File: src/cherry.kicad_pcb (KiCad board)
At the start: 2 copper layers, 51 x 21 mm, 4 parts

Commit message: wip: current layout state
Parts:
- removed H1, H2, H3, H4: MountingHole, Cherry:MountingHole_2.1mm_M2
- added C1: 10uF, Cherry:C_0805_2012Metric, F.Cu at (110.1, 83.0)
- added C10: 100nF, Cherry:C_0402_1005Metric, F.Cu at (120.2, 81.3)
- added C11: 100nF, Cherry:C_0402_1005Metric, F.Cu at (122.4, 81.3)
- added C12: 100nF, Cherry:C_0402_1005Metric, F.Cu at (118.0, 81.3)
- added C13: 100nF, Cherry:C_0402_1005Metric, F.Cu at (128.5, 83.4)
- added C14: 100nF, Cherry:C_0402_1005Metric, F.Cu at (130.7, 83.4)
- added C15: 10uF, Cherry:C_0805_2012Metric, F.Cu at (118.6, 83.4)
- added C16: 100nF, Cherry:C_0402_1005Metric, F.Cu at (124.6, 97.5)
- added C17: 100nF, Cherry:C_0402_1005Metric, F.Cu at (135.3, 95.9)
- added C18: 100nF, Cherry:C_0402_1005Metric, F.Cu at (137.5, 95.9)
- added C19: 10uF, Cherry:C_0805_2012Metric, F.Cu at (137.1, 98.2)
- added C2: 10uF, Cherry:C_0805_2012Metric, F.Cu at (110.1, 98.0)
- added C20: 100nF, Cherry:C_0402_1005Metric, F.Cu at (135.3, 85.1)
- added C21: 100nF, Cherry:C_0402_1005Metric, F.Cu at (137.5, 85.1)
- added C22: 100nF, Cherry:C_0402_1005Metric, F.Cu at (139.7, 85.1)
- added C23: 100nF, Cherry:C_0402_1005Metric, F.Cu at (141.9, 85.1)
- added C24: 100nF, Cherry:C_0402_1005Metric, F.Cu at (143.3, 82.5)
- added C25: 10uF, Cherry:C_0805_2012Metric, F.Cu at (135.9, 82.5)
- added C26: 100nF, Cherry:C_0402_1005Metric, F.Cu at (140.0, 98.2)
- added C27: 10uF, Cherry:C_0603_1608Metric, F.Cu at (142.8, 98.2)
- added C28: 100nF, Cherry:C_0402_1005Metric, F.Cu at (131.4, 95.2)
- added C3: 22uF, Cherry:C_0805_2012Metric, F.Cu at (110.1, 86.6)
- added C4: 22uF, Cherry:C_0805_2012Metric, F.Cu at (110.1, 94.4)
- added C5: 4.7uF, Cherry:C_0603_1608Metric, F.Cu at (125.7, 83.4)
- added C6: 100nF, Cherry:C_0402_1005Metric, F.Cu at (126.8, 97.5)
- added C7: 100nF, Cherry:C_0402_1005Metric, F.Cu at (129.0, 97.5)
- added C8: 100nF, Cherry:C_0402_1005Metric, F.Cu at (131.2, 97.5)
- added C9: 100nF, Cherry:C_0402_1005Metric, F.Cu at (133.4, 97.5)
- added D1: PWR, Cherry:LED_0603_1608Metric, F.Cu at (103.5, 83.8)
- added D2: CFG, Cherry:LED_0603_1608Metric, F.Cu at (103.5, 97.2)
- added D3: USER0, Cherry:LED_0603_1608Metric, F.Cu at (158.7, 89.5)
- added D4: USER1, Cherry:LED_0603_1608Metric, F.Cu at (158.7, 91.5)
- added FB1: BLM21AG601SH1D, Cherry:L_0805_2012Metric, F.Cu at (108.4, 90.5)
- added FB2: BLM21AG601SH1D, Cherry:L_0805_2012Metric, F.Cu at (122.2, 83.4)
- added J1: USB4085-GF-A, Cherry:USB_C_Receptacle_GCT_USB4085, F.Cu at (106.1, 87.5)
- added J2: PinHeader_2x24, Cherry:PinHeader_2x24_P2.54mm_Rows22.86mm, F.Cu at (130.6, 90.5)
- added J3: PinHeader_2x06, Cherry:PinHeader_2x06_P2.54mm_Vertical, F.Cu at (148.4, 90.5)
- added J4: PinHeader_1x06, Cherry:PinHeader_1x06_P2.54mm, F.Cu at (153.4, 81.6)
- added J5: PinHeader_1x06, Cherry:PinHeader_1x06_P2.54mm, F.Cu at (153.4, 99.4)
- added L1: 1uH, Cherry:L_0805_2012Metric, F.Cu at (113.4, 86.6)
- added L2: 1uH, Cherry:L_0805_2012Metric, F.Cu at (113.4, 94.4)
- added R1: 180k, Cherry:R_0402_1005Metric, F.Cu at (112.3, 88.9)
- added R10: 10k, Cherry:R_0402_1005Metric, F.Cu at (138.9, 82.5)
- added R11: 10k, Cherry:R_0402_1005Metric, F.Cu at (131.4, 85.9)
- added R12: 10k, Cherry:R_0402_1005Metric, F.Cu at (155.4, 92.9)
- added R13: 100, Cherry:R_0402_1005Metric, F.Cu at (139.7, 95.9)
- added R14: 1k, Cherry:R_0402_1005Metric, F.Cu at (106.0, 83.8)
- added R15: 1k, Cherry:R_0402_1005Metric, F.Cu at (106.0, 97.2)
- added R16: 1k, Cherry:R_0402_1005Metric, F.Cu at (155.9, 89.5)
- added R17: 1k, Cherry:R_0402_1005Metric, F.Cu at (155.9, 91.5)
- added R2: 39.2k, Cherry:R_0402_1005Metric, F.Cu at (114.4, 88.9)
- added R3: 100k, Cherry:R_0402_1005Metric, F.Cu at (112.3, 92.1)
- added R4: 100k, Cherry:R_0402_1005Metric, F.Cu at (114.4, 92.1)
- added R5: 5.1k, Cherry:R_0402_1005Metric, F.Cu at (108.4, 87.6)
- added R6: 5.1k, Cherry:R_0402_1005Metric, F.Cu at (108.4, 93.4)
- added R7: 12k, Cherry:R_0402_1005Metric, F.Cu at (117.8, 97.5)
- added R8: 10k, Cherry:R_0402_1005Metric, F.Cu at (124.6, 81.3)
- added R9: 10k, Cherry:R_0402_1005Metric, F.Cu at (141.1, 82.5)
- added SW1: RESET, Cherry:SW_Push_1P1T_NO_CK_KMR2, F.Cu at (157.6, 85.6)
- added SW2: USER, Cherry:SW_Push_1P1T_NO_CK_KMR2, F.Cu at (157.6, 95.4)
- added U1: FT2232HQ, Cherry:QFN-64-1EP_9x9mm_P0.5mm_EP4.35x4.35mm, F.Cu at (121.7, 90.5)
- added U2: ICE40LP8K-CM81, Cherry:BGA-81_9x9_8.0x8.0mm_P0.8mm, F.Cu at (139.0, 90.5)
- added U3: W25Q32JVSSIQ, Cherry:SOIC-8_3.9x4.9mm_P1.27mm, F.Cu at (131.4, 90.5)
- added U4: TPS62A02, Cherry:SOT-23-6, F.Cu at (113.4, 83.0)
- added U5: TPS62A02, Cherry:SOT-23-6, F.Cu at (113.4, 98.0)
- added X1: ASE-12.000MHZ-LC-T, Cherry:Oscillator_SMD_Abracon_ASE-4Pin_3.2x2.5mm, F.Cu at (121.2, 97.5)
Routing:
- removed copper zone on B.Cu, net GND
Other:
- board size 51 x 21 mm -> 61.2 x 26.1 mm

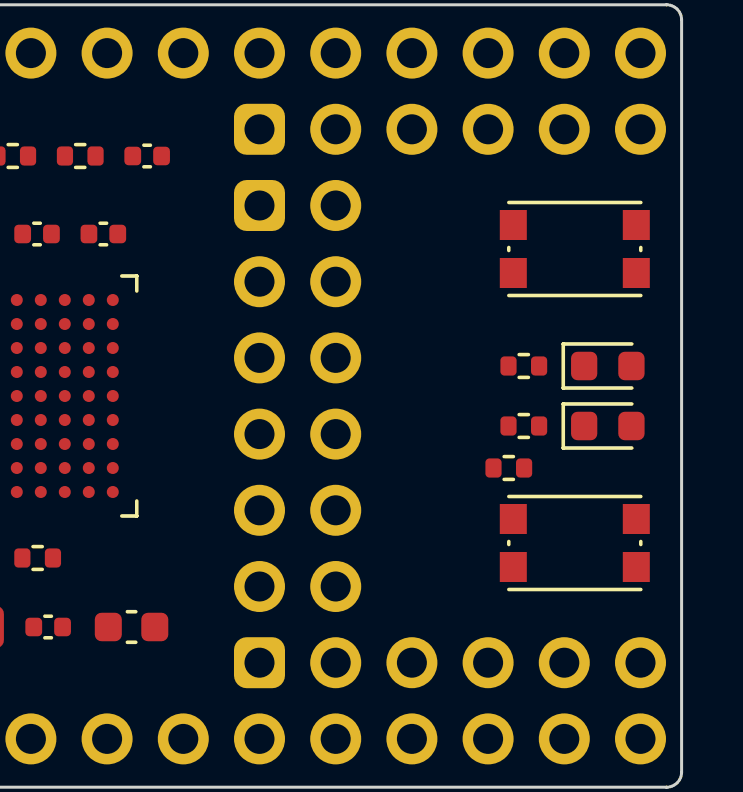
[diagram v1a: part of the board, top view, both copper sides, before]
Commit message: layout: J3を基板右端へ移動、SW/LEDを内側に再配置
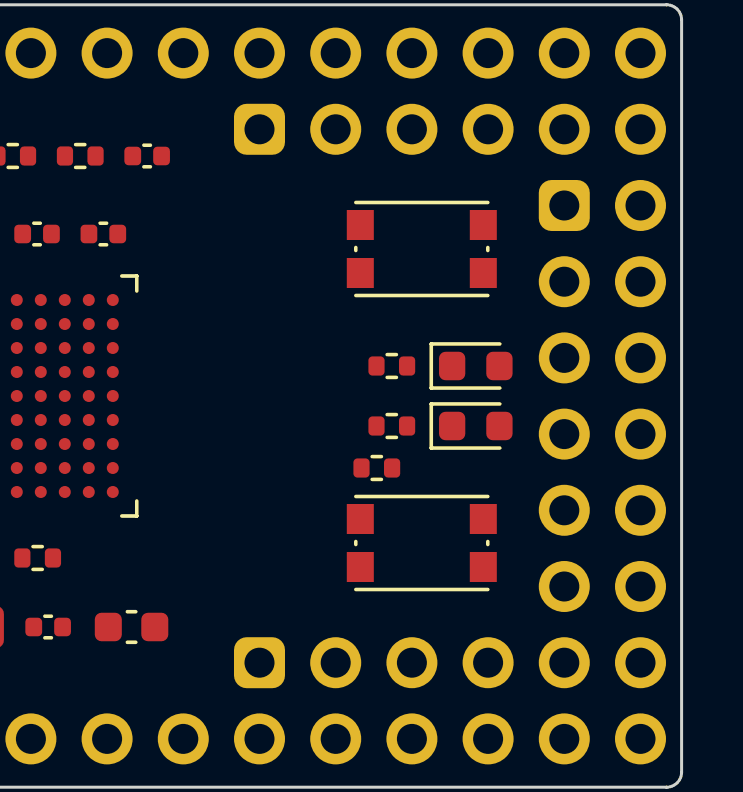
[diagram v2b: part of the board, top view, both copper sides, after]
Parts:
- moved J3 10.2 mm to (158.5, 90.5)
- moved SW1 5.10 mm to (152.5, 85.6)
- moved SW2 5.10 mm to (152.5, 95.4)
- moved R12 4.40 mm to (151.0, 92.9)
- moved R16 4.40 mm to (151.5, 89.5)
- moved R17 4.40 mm to (151.5, 91.5)
- moved D3 4.40 mm to (154.3, 89.5)
- moved D4 4.40 mm to (154.3, 91.5)
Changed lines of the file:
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@@
 	(footprint "Cherry:R_0402_1005Metric"
 		(layer "F.Cu")
-		(at 155.9 91.5)
+		(at 151.5 91.5)
 		(descr "Resistor SMD 0402 (1005 Metric), square (rectangular) end terminal, IPC-7351 nominal, (Body size source: IPC-SM-782 page 72, https://www.pcb-3d.com/wordpress/wp-content/uploads/ipc-sm-782a_amendment_1_and_2.pdf)")
 		(tags "resistor")
@@
 	(footprint "Cherry:LED_0603_1608Metric"
 		(layer "F.Cu")
-		(at 158.7 89.5)
+		(at 154.3 89.5)
 		(descr "LED SMD 0603 (1608 Metric), square (rectangular) end terminal, IPC-7351 nominal, (Body size source: http://www.tortai-tech.com/upload/download/2011102023233369053.pdf)")
 		(tags "LED")
@@
 	(footprint "Cherry:PinHeader_2x06_P2.54mm_Vertical"
 		(layer "F.Cu")
-		(at 148.36 90.5)
+		(at 158.52 90.5)
 		(descr "Pin header 2x06, 2.54mm pitch, vertical, odd-even numbering, origin at center")
 		(tags "pin header 2x06")
@@
 	(footprint "Cherry:SW_Push_1P1T_NO_CK_KMR2"
 		(layer "F.Cu")
-		(at 157.6 85.6)
+		(at 152.5 85.6)
 		(descr "CK components KMR2 tactile switch http://www.ckswitches.com/media/1479/kmr2.pdf")
 		(tags "tactile switch kmr2")
@@
 	(footprint "Cherry:SW_Push_1P1T_NO_CK_KMR2"
 		(layer "F.Cu")
-		(at 157.6 95.4)
+		(at 152.5 95.4)
 		(descr "CK components KMR2 tactile switch http://www.ckswitches.com/media/1479/kmr2.pdf")
 		(tags "tactile switch kmr2")
@@
 	(footprint "Cherry:R_0402_1005Metric"
 		(layer "F.Cu")
-		(at 155.4 92.9)
+		(at 151 92.9)
 		(descr "Resistor SMD 0402 (1005 Metric), square (rectangular) end terminal, IPC-7351 nominal, (Body size source: IPC-SM-782 page 72, https://www.pcb-3d.com/wordpress/wp-content/uploads/ipc-sm-782a_amendment_1_and_2.pdf)")
 		(tags "resistor")
@@
 	(footprint "Cherry:R_0402_1005Metric"
 		(layer "F.Cu")
-		(at 155.9 89.5)
+		(at 151.5 89.5)
 		(descr "Resistor SMD 0402 (1005 Metric), square (rectangular) end terminal, IPC-7351 nominal, (Body size source: IPC-SM-782 page 72, https://www.pcb-3d.com/wordpress/wp-content/uploads/ipc-sm-782a_amendment_1_and_2.pdf)")
 		(tags "resistor")
@@
 	(footprint "Cherry:LED_0603_1608Metric"
 		(layer "F.Cu")
-		(at 158.7 91.5)
+		(at 154.3 91.5)
 		(descr "LED SMD 0603 (1608 Metric), square (rectangular) end terminal, IPC-7351 nominal, (Body size source: http://www.tortai-tech.com/upload/download/2011102023233369053.pdf)")
 		(tags "LED")

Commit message: J3のピンヘッダを2x6から6x1に変更
未接続のデバッグ用ヘッダーJ3をPinHeader_2x06からPinHeader_1x06 (J4/J5と同じフットプリント)に変更し、board.pngを再生成。
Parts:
- J3: value PinHeader_2x06 -> PinHeader_1x06; footprint Cherry:PinHeader_2x06_P2.54mm_Vertical -> Cherry:PinHeader_1x06_P2.54mm
- turned J3 to 90 degrees
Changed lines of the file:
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@@
 		(embedded_fonts no)
 	)
-	(footprint "Cherry:PinHeader_2x06_P2.54mm_Vertical"
+	(footprint "Cherry:PinHeader_1x06_P2.54mm"
 		(layer "F.Cu")
-		(at 158.52 90.5)
-		(descr "Pin header 2x06, 2.54mm pitch, vertical, odd-even numbering, origin at center")
-		(tags "pin header 2x06")
+		(at 158.52 90.5 90)
+		(descr "Pin header 1x06, 2.54mm pitch, vertical, origin at center")
+		(tags "pin header 1x06")
 		(property "Reference" "J3"
-			(at 0 -8.8 0)
+			(at 0 -2.3 0)
 			(layer "F.Fab")
 			(effects
@@
 			)
 		)
-		(property "Value" "PinHeader_2x06"
-			(at 0 8.8 0)
+		(property "Value" "PinHeader_1x06"
+			(at 0 2.3 0)
 			(layer "F.Fab")
 			(effects
@@
 		(duplicate_pad_numbers_are_jumpers no)
 		(fp_rect
-			(start -2.5 -7.58)
-			(end 2.5 7.58)
+			(start -7.58 -1.23)
+			(end 7.58 1.23)
 			(stroke
 				(width 0.05)
@@
 		)
 		(fp_rect
-			(start -2.54 -7.62)
-			(end 2.54 7.62)
+			(start -7.62 -1.27)
+			(end 7.62 1.27)
 			(stroke
 				(width 0.1)
@@
 		)
 		(pad "1" thru_hole roundrect
-			(at -1.27 -6.35)
+			(at -6.35 0)
 			(size 1.7 1.7)
 			(drill 1)
@@
 		)
 		(pad "2" thru_hole circle
-			(at 1.27 -6.35)
+			(at -3.81 0)
 			(size 1.7 1.7)
 			(drill 1)
@@
 		)
 		(pad "3" thru_hole circle
-			(at -1.27 -3.81)
+			(at -1.27 0)
 			(size 1.7 1.7)
 			(drill 1)
@@
 		)
 		(pad "4" thru_hole circle
-			(at 1.27 -3.81)
+			(at 1.27 0)
 			(size 1.7 1.7)
 			(drill 1)
@@
 		)
 		(pad "5" thru_hole circle
-			(at -1.27 -1.27)
+			(at 3.81 0)
 			(size 1.7 1.7)
 			(drill 1)
@@
 		)
 		(pad "6" thru_hole circle
-			(at 1.27 -1.27)
+			(at 6.35 0)
 			(size 1.7 1.7)
 			(drill 1)
-			(layers "*.Cu" "*.Mask")
-			(remove_unused_layers no)
-		)
-		(pad "7" thru_hole circle
-			(at -1.27 1.27)
-			(size 1.7 1.7)
-			(drill 1)
-			(layers "*.Cu" "*.Mask")
-			(remove_unused_layers no)
-		)
-		(pad "8" thru_hole circle
-			(at 1.27 1.27)
-			(size 1.7 1.7)
-			(drill 1)
-			(layers "*.Cu" "*.Mask")
-			(remove_unused_layers no)
-		)
-		(pad "9" thru_hole circle
-			(at -1.27 3.81)
-			(size 1.7 1.7)
-			(drill 1)
-			(layers "*.Cu" "*.Mask")
-			(remove_unused_layers no)
-		)
-		(pad "10" thru_hole circle
-			(at 1.27 3.81)
-			(size 1.7 1.7)
-			(drill 1)
-			(layers "*.Cu" "*.Mask")
-			(remove_unused_layers no)
-		)
-		(pad "11" thru_hole circle
-			(at -1.27 6.35)
-			(size 1.7 1.7)
-			(drill 1)
-			(layers "*.Cu" "*.Mask")
-			(remove_unused_layers no)
-		)
-		(pad "12" thru_hole circle
-			(at 1.27 6.35)
-			(size 1.7 1.7)
-			(drill 1)

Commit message: J3ピンヘッダを基板右端に近づける
パッド銅箔と基板端のクリアランスを0.5mmまで詰めてJ3(1x06)を基板端側へ移動。
基板外形(Edge.Cuts)は変更していないため、J2の2.54mmグリッドからは外れる。
J4/J5はJ2の実ピン列を基準にすると元々グリッド一致していたため変更なし。
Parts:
- moved J3 1.29 mm to (159.8, 90.5)
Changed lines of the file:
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@@
 	(footprint "Cherry:PinHeader_1x06_P2.54mm"
 		(layer "F.Cu")
-		(at 158.52 90.5 90)
+		(at 159.81 90.5 90)
 		(descr "Pin header 1x06, 2.54mm pitch, vertical, origin at center")
 		(tags "pin header 1x06")

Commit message: wip
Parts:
- added J6: PinHeader_1x24, Cherry:PinHeader_1x24_P2.54mm, B.Cu at (159.8, 79.1)
- J2: value PinHeader_2x24 -> PinHeader_1x24; footprint Cherry:PinHeader_2x24_P2.54mm_Rows22.86mm -> Cherry:PinHeader_1x24_P2.54mm; moved to B.Cu
- J3, J4, J5: moved to B.Cu
- R10: value 10k -> 1k
- moved J2 31.4 mm to (101.4, 101.9), turned to -90 degrees
- moved J5 18.9 mm to (147.1, 81.6), turned to -90 degrees
- moved J4 16.5 mm to (159.8, 96.8)
- moved J3 15.5 mm to (147.1, 99.4), turned to -90 degrees
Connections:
- net /GPIO_19 renamed /GPIO_32
- net /GPIO_20 renamed /GPIO_31
- net /GPIO_21 renamed /GPIO_30
- net /GPIO_22 renamed /GPIO_29
- U2 pad A2: /GPIO_27 -> /GPIO_23
- U2 pad A4: /GPIO_23 -> /GPIO_27
- U2 pad A7: /GPIO_18 -> /GPIO_33
- U2 pad A8: /GPIO_16 -> /GPIO_35
- U2 pad B1: /GPIO_0 -> /GPIO_4
- U2 pad B2: /GPIO_2 -> /GPIO_6
- U2 pad B3: /GPIO_26 -> /GPIO_24
- U2 pad B4: /GPIO_24 -> /GPIO_26
- U2 pad B8: /GPIO_17 -> /GPIO_34
- U2 pad C1: /GPIO_1 -> /GPIO_5
- U2 pad C2: /GPIO_3 -> /GPIO_7
- U2 pad C9: /GPIO_9 -> /GPIO_13
- U2 pad D1: /GPIO_4 -> /GPIO_8
- U2 pad D2: /GPIO_5 -> /GPIO_9
- U2 pad D9: /GPIO_8 -> /GPIO_12
- U2 pad E1: /GPIO_6 -> /GPIO_10
- U2 pad E2: /GPIO_7 -> /GPIO_11
- U2 pad F1: /GPIO_10 -> /GPIO_14
- U2 pad G9: /GPIO_11 -> /GPIO_15
- U2 pad H1: /GPIO_12 -> /GPIO_16
- U2 pad J1: /GPIO_13 -> /GPIO_17
- U2 pad J2: /GPIO_14 -> /GPIO_18
- U2 pad J3: /GPIO_15 -> /GPIO_36

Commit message: passive
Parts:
- added R18: 470, Cherry:R_0402_1005Metric, F.Cu at (134.0, 95.2)
- added R19: 470, Cherry:R_0402_1005Metric, F.Cu at (135.3, 95.2)
- added R20: 470, Cherry:R_0402_1005Metric, F.Cu at (136.5, 95.2)
- added R21: 470, Cherry:R_0402_1005Metric, F.Cu at (137.8, 95.2)
- added R22: 1k, Cherry:R_0402_1005Metric, F.Cu at (132.7, 96.5)
- moved C11 16.1 mm to (125.1, 97.2)
- moved X1 16.0 mm to (115.6, 82.5)
- moved C20 15.7 mm to (146.7, 95.9)
- moved C9 14.7 mm to (126.6, 84.5)
- moved R8 14.7 mm to (120.0, 95.2)
- moved C21 14.5 mm to (149.9, 92.6), turned to 90 degrees
- moved R9 13.8 mm to (153.7, 88.3)
- moved C18 13.1 mm to (144.8, 85.0)
- moved C19 13.0 mm to (149.9, 95.9)
- moved J5 12.9 mm to (160.0, 81.3), turned to 90 degrees
- moved C26 12.7 mm to (149.9, 90.2), turned to 90 degrees
- moved C4 12.1 mm to (121.3, 99.1), turned to 0 degrees
- moved C14 11.8 mm to (121.2, 90.4), turned to 90 degrees
- moved C27 11.7 mm to (151.3, 90.2), turned to 90 degrees
- moved C10 11.7 mm to (121.2, 92.9), turned to 90 degrees
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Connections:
- D1 pad 1: Net-(D1-A) -> GND
- D1 pad 2: +3V3 -> Net-(D1-A)
- D2 pad 1: /CDONE -> GND
- J2 pad 1: (no net) -> +5V
- J2 pad 10: (no net) -> /GPIO_4
- J2 pad 11: (no net) -> /GPIO_5
- J2 pad 12: (no net) -> /GPIO_6
- J2 pad 13: (no net) -> /GPIO_7
- J2 pad 14: (no net) -> /GPIO_8
- J2 pad 15: (no net) -> /GPIO_9
- J2 pad 16: (no net) -> /GPIO_10
- J2 pad 17: (no net) -> /GPIO_11
- J2 pad 18: (no net) -> /GPIO_12
- J2 pad 19: (no net) -> /GPIO_13
- J2 pad 2: (no net) -> +3V3
- J2 pad 20: (no net) -> /GPIO_14
- J2 pad 21: (no net) -> /GPIO_15
- J2 pad 22: (no net) -> /GPIO_16
- J2 pad 23: (no net) -> /GPIO_17
- J2 pad 24: (no net) -> /GPIO_18
- J2 pad 3: (no net) -> GND
- J2 pad 4: (no net) -> GND
- J2 pad 5: (no net) -> GND
- J2 pad 6: (no net) -> /CRESET_B
- J2 pad 7: (no net) -> /GPIO_1
- J2 pad 8: (no net) -> /GPIO_2
- J2 pad 9: (no net) -> /GPIO_3
- J3 pad 1: (no net) -> /GPIO_37
- J3 pad 2: (no net) -> /GPIO_38
- J3 pad 3: (no net) -> /GPIO_39
- J3 pad 4: (no net) -> /GPIO_40
- J3 pad 5: (no net) -> /GPIO_41
- J3 pad 6: (no net) -> /GPIO_42
- J4 pad 1: (no net) -> /GPIO_43
- J4 pad 2: (no net) -> /GPIO_44
- J4 pad 3: (no net) -> /GPIO_45
- J4 pad 4: (no net) -> /GPIO_46
- J4 pad 5: (no net) -> /GPIO_47
- J4 pad 6: (no net) -> /GPIO_48
- J5 pad 1: (no net) -> /GPIO_49
- J5 pad 2: (no net) -> /GPIO_50
- J5 pad 3: (no net) -> /GPIO_51
- J5 pad 4: (no net) -> /GPIO_52
- J5 pad 5: (no net) -> /GPIO_53
- J5 pad 6: (no net) -> GND
- J6 pad 1: (no net) -> /GPIO_19
- J6 pad 10: (no net) -> /GPIO_28
- J6 pad 11: (no net) -> /GPIO_29
- J6 pad 12: (no net) -> /GPIO_30
- J6 pad 13: (no net) -> /GPIO_31
- J6 pad 14: (no net) -> /GPIO_32
- J6 pad 15: (no net) -> /GPIO_33
- J6 pad 16: (no net) -> /GPIO_34
- J6 pad 17: (no net) -> /GPIO_35
- J6 pad 18: (no net) -> /GPIO_36
- J6 pad 19: (no net) -> GND
- J6 pad 2: (no net) -> /GPIO_20
- J6 pad 20: (no net) -> GND
- J6 pad 21: (no net) -> GND
- J6 pad 22: (no net) -> GND
- J6 pad 23: (no net) -> +3V3
- J6 pad 24: (no net) -> +5V
- J6 pad 3: (no net) -> /GPIO_21
- J6 pad 4: (no net) -> /GPIO_22
- J6 pad 5: (no net) -> /GPIO_23
- J6 pad 6: (no net) -> /GPIO_24
- J6 pad 7: (no net) -> /GPIO_25
- J6 pad 8: (no net) -> /GPIO_26
- J6 pad 9: (no net) -> /GPIO_27
- R14 pad 1: Net-(D1-A) -> +3V3
- R14 pad 2: GND -> Net-(D1-A)
- R15 pad 1: +3V3 -> /CDONE
- R8 pad 2: /FT_RESET -> Net-(U1-~{RESET})
- U1 pad 1: (no net) -> GND
- U1 pad 10: (no net) -> GND
- U1 pad 11: (no net) -> GND
- U1 pad 12: (no net) -> /VCORE
- U1 pad 13: (no net) -> GND
- U1 pad 14: (no net) -> Net-(U1-~{RESET})
- U1 pad 15: (no net) -> GND
- U1 pad 16: (no net) -> /FT_SCK
- U1 pad 17: (no net) -> /FT_MOSI
- U1 pad 18: (no net) -> /FT_MISO
- U1 pad 19: (no net) -> unconnected-(U1-ADBUS3-Pad19)
- U1 pad 2: (no net) -> /CLK_12M
- U1 pad 20: (no net) -> +3V3
- U1 pad 21: (no net) -> /FT_SS
- U1 pad 22: (no net) -> unconnected-(U1-ADBUS5-Pad22)
- U1 pad 23: (no net) -> /CDONE
- U1 pad 24: (no net) -> /FT_CRESET
- U1 pad 25: (no net) -> GND
- U1 pad 26: (no net) -> unconnected-(U1-ACBUS0-Pad26)
- U1 pad 27: (no net) -> unconnected-(U1-ACBUS1-Pad27)
- U1 pad 28: (no net) -> unconnected-(U1-ACBUS2-Pad28)
- U1 pad 29: (no net) -> unconnected-(U1-ACBUS3-Pad29)
- U1 pad 3: (no net) -> unconnected-(U1-OSCO-Pad3)
- U1 pad 30: (no net) -> unconnected-(U1-ACBUS4-Pad30)
- U1 pad 31: (no net) -> +3V3
- U1 pad 32: (no net) -> unconnected-(U1-ACBUS5-Pad32)
- U1 pad 33: (no net) -> unconnected-(U1-ACBUS6-Pad33)
- U1 pad 34: (no net) -> unconnected-(U1-ACBUS7-Pad34)
- U1 pad 35: (no net) -> GND
- U1 pad 36: (no net) -> unconnected-(U1-~{SUSPEND}-Pad36)
- U1 pad 37: (no net) -> /VCORE
- U1 pad 38: (no net) -> /UART_TX
- U1 pad 39: (no net) -> /UART_RX
- U1 pad 4: (no net) -> /+3V3A
- U1 pad 40: (no net) -> unconnected-(U1-BDBUS2-Pad40)
- U1 pad 41: (no net) -> unconnected-(U1-BDBUS3-Pad41)
- U1 pad 42: (no net) -> +3V3
- U1 pad 43: (no net) -> unconnected-(U1-BDBUS4-Pad43)
- U1 pad 44: (no net) -> unconnected-(U1-BDBUS5-Pad44)
- U1 pad 45: (no net) -> unconnected-(U1-BDBUS6-Pad45)
- U1 pad 46: (no net) -> unconnected-(U1-BDBUS7-Pad46)
- U1 pad 47: (no net) -> GND
- U1 pad 48: (no net) -> unconnected-(U1-BCBUS0-Pad48)
- U1 pad 49: (no net) -> /VCORE
- U1 pad 5: (no net) -> GND
- U1 pad 50: (no net) -> +3V3
- U1 pad 51: (no net) -> GND
- U1 pad 52: (no net) -> unconnected-(U1-BCBUS1-Pad52)
- U1 pad 53: (no net) -> unconnected-(U1-BCBUS2-Pad53)
- U1 pad 54: (no net) -> unconnected-(U1-BCBUS3-Pad54)
- U1 pad 55: (no net) -> unconnected-(U1-BCBUS4-Pad55)
- U1 pad 56: (no net) -> +3V3
- U1 pad 57: (no net) -> unconnected-(U1-BCBUS5-Pad57)
- U1 pad 58: (no net) -> unconnected-(U1-BCBUS6-Pad58)
- U1 pad 59: (no net) -> unconnected-(U1-BCBUS7-Pad59)
- U1 pad 6: (no net) -> Net-(U1-REF)
- U1 pad 60: (no net) -> unconnected-(U1-~{PWREN}-Pad60)
- U1 pad 61: (no net) -> unconnected-(U1-EEDATA-Pad61)
- U1 pad 62: (no net) -> unconnected-(U1-EECLK-Pad62)
- U1 pad 63: (no net) -> unconnected-(U1-EECS-Pad63)
- U1 pad 64: (no net) -> /VCORE
- U1 pad 65: (no net) -> GND
- U1 pad 7: (no net) -> /USB_DM
- U1 pad 8: (no net) -> /USB_DP
- U1 pad 9: (no net) -> /+3V3A
- U2 pad A1: unconnected-(U2-IOT_224-PadA1) -> /GPIO_34
- U2 pad A2: /GPIO_23 -> /GPIO_33
- U2 pad A3: /GPIO_25 -> /GPIO_31
- U2 pad A6: /GPIO_31 -> /GPIO_24
- U2 pad A7: /GPIO_33 -> /GPIO_21
- U2 pad A8: /GPIO_35 -> /GPIO_20
- U2 pad A9: unconnected-(U2-IOR_116-PadA9) -> /GPIO_46
- U2 pad B1: /GPIO_4 -> /GPIO_3
- U2 pad B2: /GPIO_6 -> /GPIO_2
- U2 pad B3: /GPIO_24 -> /GPIO_32
- U2 pad B4: /GPIO_26 -> /GPIO_28
- U2 pad B5: /GPIO_29 -> /GPIO_25
- U2 pad B6: /GPIO_30 -> /GPIO_23
- U2 pad B7: /GPIO_32 -> /GPIO_22
- U2 pad B8: /GPIO_34 -> /GPIO_19
- U2 pad B9: unconnected-(U2-IOR_120-PadB9) -> /GPIO_50
- U2 pad C1: /GPIO_5 -> /GPIO_4
- U2 pad C2: /GPIO_7 -> /GPIO_1
- U2 pad C3: unconnected-(U2-IOL_7B-PadC3) -> /GPIO_6
- U2 pad C4: /CLK_12M -> /BTN
- U2 pad C5: unconnected-(U2-IOT_197_GBIN1-PadC5) -> /GPIO_26
- U2 pad C9: /GPIO_13 -> /GPIO_53
- U2 pad D1: /GPIO_8 -> /GPIO_7
- U2 pad D2: /GPIO_9 -> /GPIO_5
- U2 pad D3: unconnected-(U2-IOL_13B_GBIN7-PadD3) -> /GPIO_10
- U2 pad D5: unconnected-(U2-IOT_212-PadD5) -> /GPIO_29
- U2 pad D6: unconnected-(U2-IOR_115-PadD6) -> /GPIO_45
- U2 pad D7: unconnected-(U2-IOR_117-PadD7) -> /GPIO_47
- U2 pad D8: unconnected-(U2-IOR_141_GBIN2-PadD8) -> /GPIO_52
- U2 pad D9: /GPIO_12 -> /GPIO_49
- U2 pad E1: /GPIO_10 -> /GPIO_8
- U2 pad E2: /GPIO_11 -> /GPIO_9
- U2 pad E3: unconnected-(U2-IOL_14A_GBIN6-PadE3) -> /GPIO_11
- U2 pad E4: unconnected-(U2-IOL_14B-PadE4) -> /GPIO_12
- U2 pad E5: unconnected-(U2-IOT_214-PadE5) -> /GPIO_30
- U2 pad E7: unconnected-(U2-IOR_118-PadE7) -> /GPIO_48
- U2 pad E8: unconnected-(U2-IOR_140_GBIN3-PadE8) -> /GPIO_51
- U2 pad F1: /GPIO_14 -> /GPIO_13
- U2 pad F3: unconnected-(U2-IOL_22B-PadF3) -> /GPIO_14
- U2 pad F8: unconnected-(U2-IOR_113-PadF8) -> /GPIO_43
- U2 pad G1: unconnected-(U2-IOL_24B-PadG1) -> /GPIO_16
- U2 pad G2: unconnected-(U2-IOL_26A-PadG2) -> /GPIO_17
- U2 pad G3: unconnected-(U2-IOL_24A-PadG3) -> /GPIO_15
- U2 pad G4: unconnected-(U2-IOB_81_GBIN5-PadG4) -> /CLK_12M
- U2 pad G5: unconnected-(U2-IOB_103_CBSEL0-PadG5) -> /GPIO_40
- U2 pad G8: unconnected-(U2-IOR_114-PadG8) -> /GPIO_44
- U2 pad G9: /GPIO_15 -> /GPIO_42
- U2 pad H1: /GPIO_16 -> /GPIO_35
- U2 pad H2: unconnected-(U2-IOL_26B-PadH2) -> /GPIO_18
- U2 pad H4: /BTN -> /GPIO_39
- U2 pad H5: unconnected-(U2-IOB_104_CBSEL1-PadH5) -> /GPIO_41
- U2 pad J1: /GPIO_17 -> /GPIO_36
- U2 pad J2: /GPIO_18 -> /GPIO_37
- U2 pad J3: /GPIO_36 -> /GPIO_38
- U2 pad J4: /UART_TX -> /LED0
- U2 pad J8: /LED0 -> /UART_TX
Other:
- board text added: "NextMicon Cherry v1"
- board text removed: "Cherry"

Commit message: layout
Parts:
- moved R10 19.1 mm to (128.1, 97.8)
- moved C11 13.5 mm to (123.2, 83.8), turned to 180 degrees
- moved C22 9.28 mm to (149.9, 84.5)
- moved C3 8.84 mm to (118.1, 90.2), turned to -90 degrees
- moved FB2 8.42 mm to (115.6, 83.2), turned to 90 degrees
- moved C19 8.30 mm to (141.6, 95.9)
- moved C1 7.65 mm to (109.2, 90.2), turned to -90 degrees
- moved FB1 7.01 mm to (109.2, 83.2), turned to 90 degrees
- moved R22 6.98 mm to (125.7, 96.5), turned to 180 degrees
- moved C25 5.89 mm to (141.6, 84.5)
- moved R7 5.85 mm to (120.7, 87.6), turned to 90 degrees
- moved C16 5.75 mm to (125.7, 97.8)
- moved C4 3.70 mm to (118.1, 97.2), turned to 90 degrees
- moved X1 3.24 mm to (112.4, 83.2), turned to 90 degrees
- moved C13 2.88 mm to (120.7, 85.1)
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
